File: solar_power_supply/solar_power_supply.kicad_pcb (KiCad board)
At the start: 2 copper layers, 46 x 17.9 mm, 16 parts, among them J1 Conn_01x02_Pin, J2 Conn_01x02_Pin, J3 Conn_01x02_Pin, J4 Conn_01x02_Pin, Q1 2N7002, U1 AP3015AKTR-G1

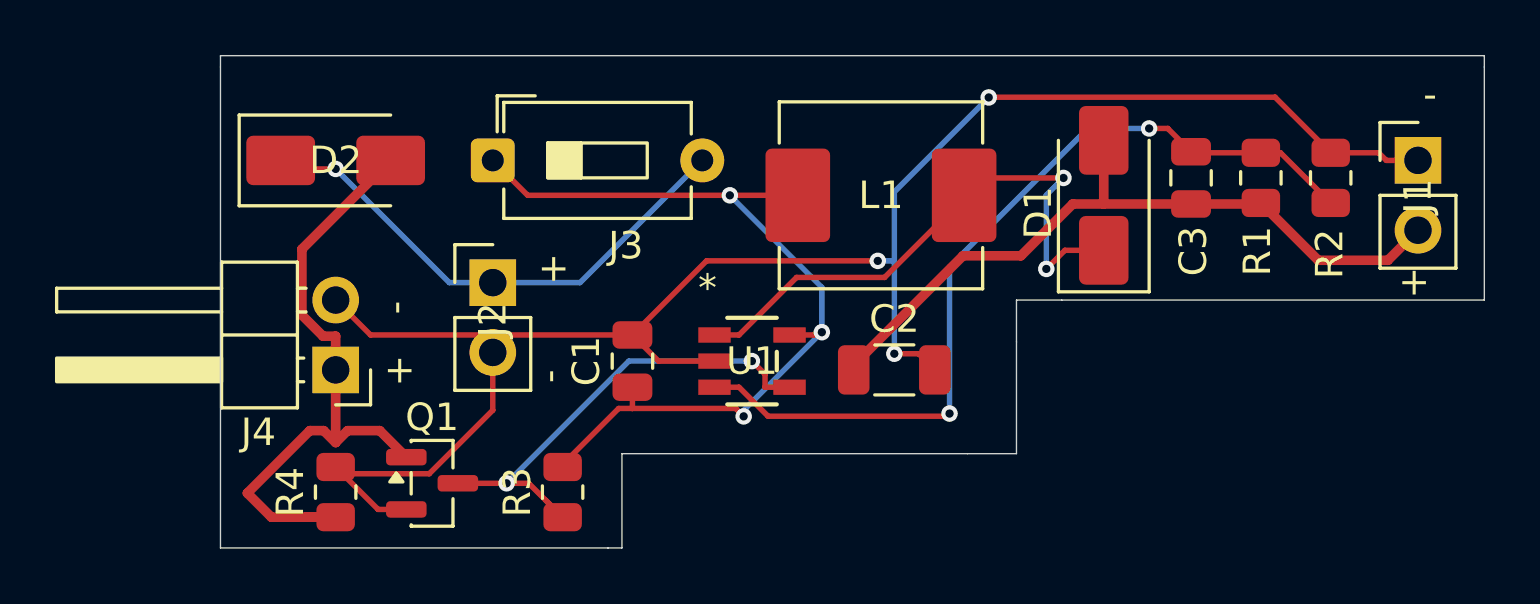
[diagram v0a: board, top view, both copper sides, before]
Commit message: solar PS copper fills
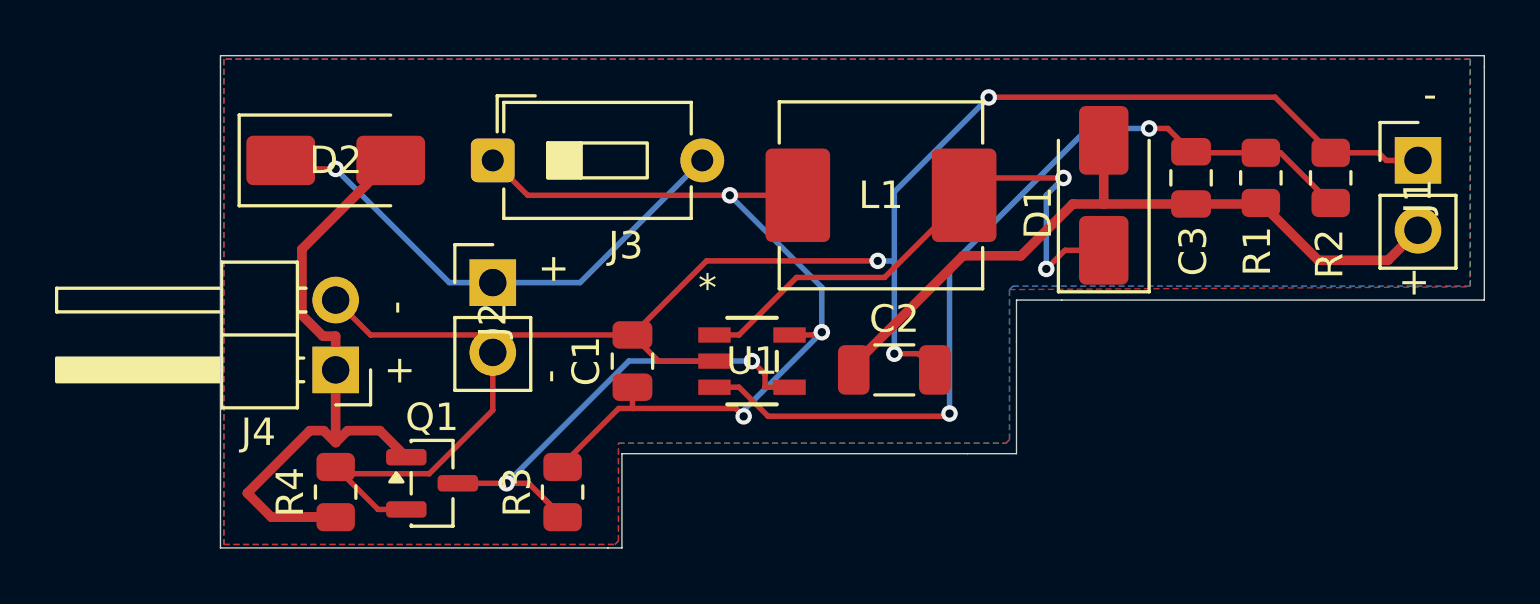
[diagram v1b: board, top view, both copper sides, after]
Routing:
- added copper zone on B.Cu, net GNDD
- added copper zone on F.Cu, net GNDD
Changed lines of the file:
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@@
 		(net 8)
+	)
+	(zone
+		(net 1)
+		(net_name "GNDD")
+		(layer "F.Cu")
+		(name "front copper")
+		(hatch edge 0.5)
+		(connect_pads
+			(clearance 0.5)
+		)
+		(min_thickness 0.25)
+		(filled_areas_thickness no)
+		(fill yes
+			(thermal_gap 0.5)
+			(thermal_bridge_width 0.5)
+		)
+		(polygon
+			(pts
+				(xy 114.681 85.217) (xy 114.681 102.87) (xy 128.905 102.87) (xy 129.032 102.743) (xy 129.032 99.187)
+				(xy 143.129 99.187) (xy 143.256 99.06) (xy 143.256 93.599) (xy 160 93.5) (xy 160 85.217)
+			)
+		)
+	)
+	(zone
+		(net 1)
+		(net_name "GNDD")
+		(layer "B.Cu")
+		(name "back copper")
+		(hatch edge 0.5)
+		(priority 1)
+		(connect_pads
+			(clearance 0.5)
+		)
+		(min_thickness 0.25)
+		(filled_areas_thickness no)
+		(fill yes
+			(thermal_gap 0.5)
+			(thermal_bridge_width 0.5)
+		)
+		(polygon
+			(pts
+				(xy 114.681 85.217) (xy 114.681 102.87) (xy 128.905 102.87) (xy 129.032 102.743) (xy 129.032 99.187)
+				(xy 143.129 99.187) (xy 143.256 99.06) (xy 143.256 93.599) (xy 143.383 93.472) (xy 160.02 93.472)
+				(xy 160.02 85.217)
+			)
+		)
 	)
 	(embedded_fonts no)
